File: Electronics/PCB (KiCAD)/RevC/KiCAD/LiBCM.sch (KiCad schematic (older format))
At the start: 237 parts, among them J1 Conn_01x08, J10 Screw_Terminal_01x03, J11 Screw_Terminal_01x08, J12 Conn_01x02, J14 Conn_01x04, J15 Conn_01x02, J19 Conn_01x02, J2 Conn_01x08, J20 Conn_01x02, J3 Conn_01x08, J4 Conn_02x06_Odd_Even, J5 Conn_01x08, J6 Conn_01x08, J7 Conn_01x08, J8 Conn_01x04, J9 Screw_Terminal_01x08, M1 Fan, M2 Fan, M3 Fan, P1 OEM_BCM_Connector, P2 Conn_WallPlug_Earth, Q1 Q_NMOS_GSD, Q2 Q_NMOS_GSD, Q3 Q_NMOS_GSD, Q4 Q_NMOS_GSD, Q5 Q_NMOS_GSD, Q6 Q_NMOS_GSD, Q7 Q_NMOS_GSD, Q73 Q_NMOS_GSD, Q74 Q_NMOS_GSD, Q75 Q_PMOS_GSD, Q76 Q_NMOS_GSD, Q77 Q_PMOS_GSD, SW2 SW_DIP_x02, U1 AP63205WU, U2 LT1487, U3 LT1487, U4 LT1797, U5 MOC3023M, U6 SFH620A-2X007T, U7 SFH620A-2X007T, U8 EPM1210SJ, U9 H11D1SR2VM

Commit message: RevC PCB in Layout
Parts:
- removed J10: Screw_Terminal_01x03, Connector_Wire:SolderWire-1sqmm_1x03_P5.4mm_D1.4mm_OD2.7mm, symbol Connector:Screw_Terminal_01x03
- removed J12, J19, J20: Conn_01x02, Connector_PinHeader_2.54mm:PinHeader_1x02_P2.54mm_Vertical, symbol Connector_Generic:Conn_01x02
- removed J4: Conn_02x06_Odd_Even, symbol Connector_Generic:Conn_02x06_Odd_Even
- removed R80: DNP, Resistor_SMD:R_0805_2012Metric, symbol Device:R
- added J10: Screw_Terminal_01x01, Connector_Wire:SolderWire-1sqmm_1x01_D1.4mm_OD2.7mm, symbol Connector:Screw_Terminal_01x01
- added J12, J19, J20: Conn_02x02, Linsight:CONN_WM26831CT-ND​, symbol Connector_Generic:Conn_02x02_Counter_Clockwise
- added J21: Conn_01x04, Connector_PinHeader_2.54mm:PinHeader_1x04_P2.54mm_Vertical, symbol Connector_Generic:Conn_01x04
- added J4: Conn_02x08_Odd_Even, Connector_PinHeader_2.54mm:PinHeader_2x08_P2.54mm_Vertical, symbol Connector_Generic:Conn_02x08_Odd_Even
- added R358: DNP, Resistor_SMD:R_0805_2012Metric, symbol LiBCM-rescue:R
- added R80: 71k5, Resistor_SMD:R_0805_2012Metric, symbol LiBCM-rescue:R
- added SW1: SW_Push, Button_Switch_Keyboard:SW_Cherry_MX_1.00u_PCB, symbol Switch:SW_Push
- BZ1: footprint (none) -> Linsight:BUZZER_WT-1205
- D18: footprint (none) -> Diode_SMD:D_SMA
- J14: footprint Connector_PinHeader_2.54mm:PinHeader_1x04_P2.54mm_Vertical -> Connector_PinSocket_2.54mm:PinSocket_1x04_P2.54mm_Horizontal
- J22: renamed from J?; footprint (none) -> Connector_PinSocket_2.54mm:PinSocket_1x08_P2.54mm_Vertical
- R328, R329: value 20 -> DNP
- R40, R41: value 100 -> DNP
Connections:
- net L1_FUSED is gone; now on net L1: D6.2 (A2), F1.1, R73.1, R74.1, R75.1, R76.2
- net +5V: now also R358.2, SW1.2
- net +5VP: now also R358.1
- net BATTSCI_DE: now also J4.1 (Pin_1)
- net BATTSCI_REn: now also J4.2 (Pin_2)
- net BUZZER: now also J4.5 (Pin_5)
- net GND_ENG: now also R63.2, R65.1, J12.3 (Pin_3), J12.4 (Pin_4), J19.3 (Pin_3), J19.4 (Pin_4), J20.3 (Pin_3), J20.4 (Pin_4), J21.4 (Pin_4), J4.15 (Pin_15), J4.16 (Pin_16), R80.2; no longer H2.1, H7.1, R63.1, R65.2
- net GRID_PWM_DIV: now also R63.1; no longer R63.2
- net L1: no longer F1.2, P2.1 (AC_P)
- net L1_GRID: now also J10.1 (Pin_1)
- net LED3: now also J4.8 (Pin_8); no longer J3.7 (Pin_7)
- net LED4: now also J4.10 (Pin_10); no longer J3.8 (Pin_8)
- net MCM_E_LED_C: now also R65.2; no longer R65.1
- net SCLc: now also J8.2 (Pin_2); no longer J8.3 (Pin_3)
- net SDAc: now also J8.3 (Pin_3); no longer J8.2 (Pin_2)
- net SPI_CS_EXT: now also J4.7 (Pin_7)
- net SPI_CS_LTC: now also J4.13 (Pin_13)
- net SPI_MISO: now also J22.4 (Pin_4), J4.12 (Pin_12)
- net SPI_MOSI: now also J22.2 (Pin_2), R317.2, R321.1, J4.11 (Pin_11); no longer R318.2, R322.1
- net SPI_MOSI_FILT: now also C162.2, R321.2; no longer C161.2, J22.3 (Pin_3), R322.2
- net SPI_SCK: now also J22.3 (Pin_3), R318.2, R322.1, J4.14 (Pin_14); no longer R317.2, R321.1
- net SPI_SCK_FILT: now also C161.2, R322.2; no longer C162.2, J22.2 (Pin_2), R321.2
- net TBATT_BAY1: now also C156.2, R14.1, R19.2, J20.1 (Pin_1); no longer C101.2, J3.2 (Pin_2), R14.2
- net TBATT_BAY2: now also C157.2, R12.1, R48.2, J19.1 (Pin_1); no longer C102.2, J3.3 (Pin_3), R12.2
- net TBATT_BAY3: now also C158.2, R4.1, R58.2, J12.1 (Pin_1); no longer C155.2, J3.4 (Pin_4), R4.2
- net TEMP_EN: now also J4.9 (Pin_9)
- net TEMP_NEG: now also J12.2 (Pin_2), J19.2 (Pin_2), J20.2 (Pin_2)
- net OP_OUT: now reaches R334.1, R67.1, U4.1 (OUT)
- net SDAd: now reaches C160.1, R313.1, R314.1
- net BUZ1: now reaches BZ1.2 (+), D16.2 (A), Q73.3 (D)
- net GPIO renamed GPIO-0
- net GPIO-0: now also J4.3 (Pin_3)
- net GRID_POSITIVE renamed GRID_HVDC+
- net LiBCM BMS/LTC6820_MISO renamed SPI_MISO_FILT
- net SPI_MISO_FILT: no longer J22.4 (Pin_4)
- new net COVER_SWITCH: J4.4 (Pin_4), R80.1, SW1.1
- new net GPIO-1: J21.1 (Pin_1), J3.7 (Pin_7)
- new net GPIO-2: J21.2 (Pin_2), J3.8 (Pin_8)
- new net GPIO-3: J21.3 (Pin_3), J4.6 (Pin_6)
- new net L1_UNFUSED: F1.2, P2.1 (AC_P)
- new net TBATT_BAY1_LPF: C101.2, J3.2 (Pin_2), R14.2
- new net TBATT_BAY2_LPF: C102.2, J3.3 (Pin_3), R12.2
- new net TBATT_BAY3_LPF: C155.2, J3.4 (Pin_4), R4.2
- no-connect marks 23 -> 25
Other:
- note added: "40(BAT_REn)"
- note added: "41(BAT_DE)"
- note added: "42(COVERSWITCH)"
- note added: "43(GPIO-0)"
- note added: "44(GPIO-3)"
- note added: "45(BUZZER)"
- note added: "46(LED3)"
- note added: "47(SS_EXT)"
- note added: "48(LED4)"
- note added: "GPIO"
- note added: "HVDC\nBATT"
- note added: "L1_GRID\n\nL2\n\nGND_EARTH"
- note added: "SPI_CS_LTC"
- note added: "THIS IS NOT AN\nINTERLOCK!!!"
- note added: "USE 250 mW COMPONENTS!\n2.4 mA @ 240AC = 576 mW\n1.2 mA @ 120AC = 144 mW"
- note added: "VCC\nSCK\nMOSI\nMISO\nGPIO-0\nCS_EXT\nGND\nGND"
- note removed: "2.4 mA @ 240AC = 576 mW\n1.2 mA @ 120AC = 144 mW"
- note removed: "44(SS_EXT)"
- note removed: "45(BAT_REn)"
- note removed: "46(BUZZER)"
- note removed: "47(BAT_DE)"
- note removed: "48(GPIO)"
- note removed: "BAY1"
- note removed: "BAY2"
- note removed: "BAY3"
- note removed: "GPIO\nSPI_CS_EXT\nSPI_CS_LTC"
- note removed: "GRID_L1\nGRID_L2(N)\nGRID_GND"
- note removed: "IMA BATTERY"
- note removed: "ONLY CONNECTS\nTO VEHICLE CHASSIS\n(PG1 & PG2)"
- note removed: "VCC\nSCK\nMOSI\nMISO\nGPIO\nCS_EXT\nGND\nGND"
- moved on the sheet: BZ1, C1, C10, C101, C102, C11, C12, C13, C14, C143, C144, C145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

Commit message: RevC PCB
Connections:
- net BATTFANH_EN: now also J3.1 (Pin_1); no longer J2.3 (Pin_3)
- net BATTFANL_EN: now also J2.8 (Pin_8); no longer J2.2 (Pin_2)
- net TURN_OFF_5V: now also J6.5 (Pin_5); no longer J3.1 (Pin_1)
- net USER_SW: now also J2.2 (Pin_2); no longer J6.5 (Pin_5)
- net VPIN_IN: now also J2.3 (Pin_3); no longer J2.8 (Pin_8)
- no-connect marks 25 -> 24
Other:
- note added: "TEMP_BLU_LPF"
- note added: "TEMP_GRN_LPF"
- note added: "TEMP_WHT_LPF"
- note added: "TEMP_YEL_LPF"
- note added: "VPIN_IN"
- moved on the sheet: C13, C170, F1, P2, Q2, R12, R14, R18, R22, R23, R27, R312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

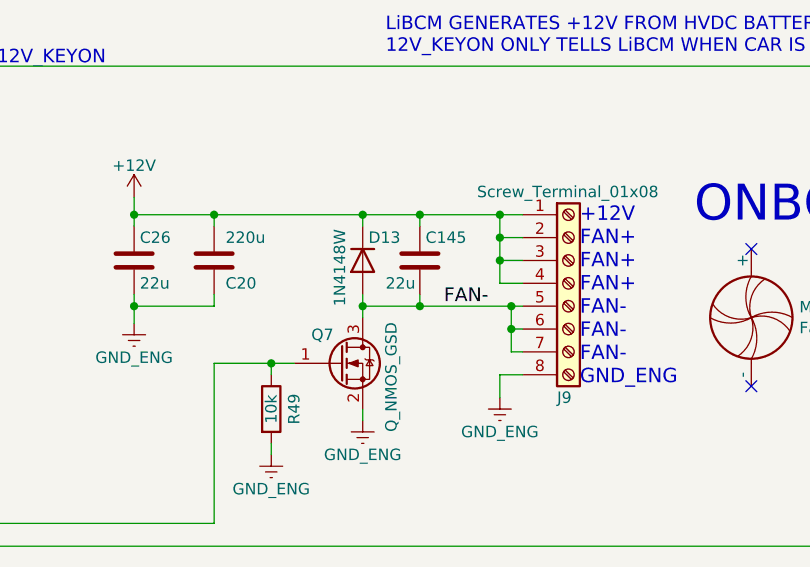
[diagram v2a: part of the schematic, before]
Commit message: Thinner Safety Cover
Also updated Fan cap to 2 uF, and generated centroids.
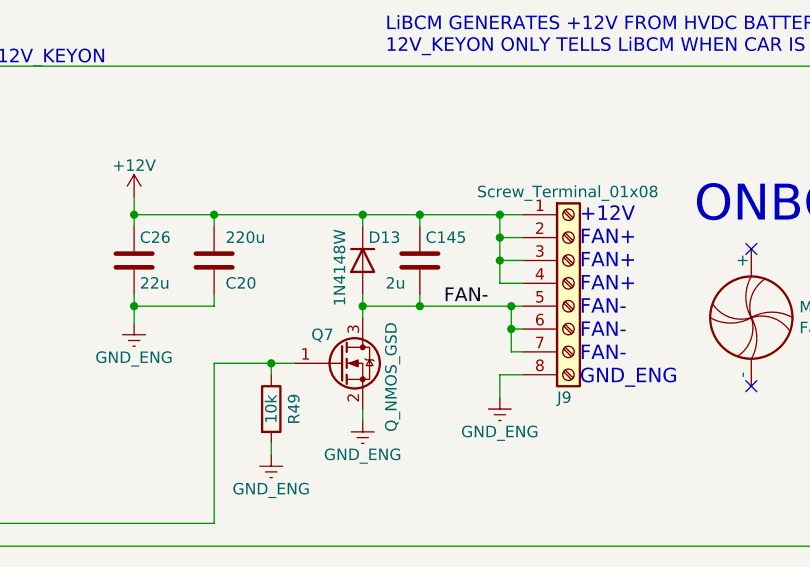
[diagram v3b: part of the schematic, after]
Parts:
- C145: value 22u -> 2u
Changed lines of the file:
@@
 P 9500 5250
 F 0 "C145" H 9525 5350 50  0000 L CNN
-F 1 "22u" H 9350 5150 50  0000 L CNN
+F 1 "2u" H 9350 5150 50  0000 L CNN
 F 2 "Capacitor_SMD:C_1210_3225Metric" H 9538 5100 50  0001 C CNN
 F 3 "" H 9500 5250 50  0000 C CNN
